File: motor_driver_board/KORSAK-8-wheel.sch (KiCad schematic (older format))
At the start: 24 parts, among them J1 Screw_Terminal_01x04, J2 Conn_01x02_Male, J3 Screw_Terminal_01x06, J4 Screw_Terminal_01x04, M1 Motor_DC, M2 Motor_DC, M3 Motor_DC, M4 Motor_DC, M5 Motor_DC, M6 Motor_DC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

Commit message: Откат прошлого коммита, т.к. это незаконченная версия
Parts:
- removed C1, C2, C3, C4, C5, C6, C7, C8: 10pF, symbol Device:C
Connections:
- net at M8.1 (+): now also U2.3 (1Y); no longer U2.6 (2Y)
- net at M8.2 (-): now also U2.6 (2Y); no longer U2.3 (1Y)
- net at U3.3 (1Y): now also M6.1 (+); no longer M6.2 (-)
- net at U3.6 (2Y): now also M6.2 (-); no longer M6.1 (+)
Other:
- moved on the sheet: J1, J4, M1, M2, M3, M4, M5, M6, M7, M8

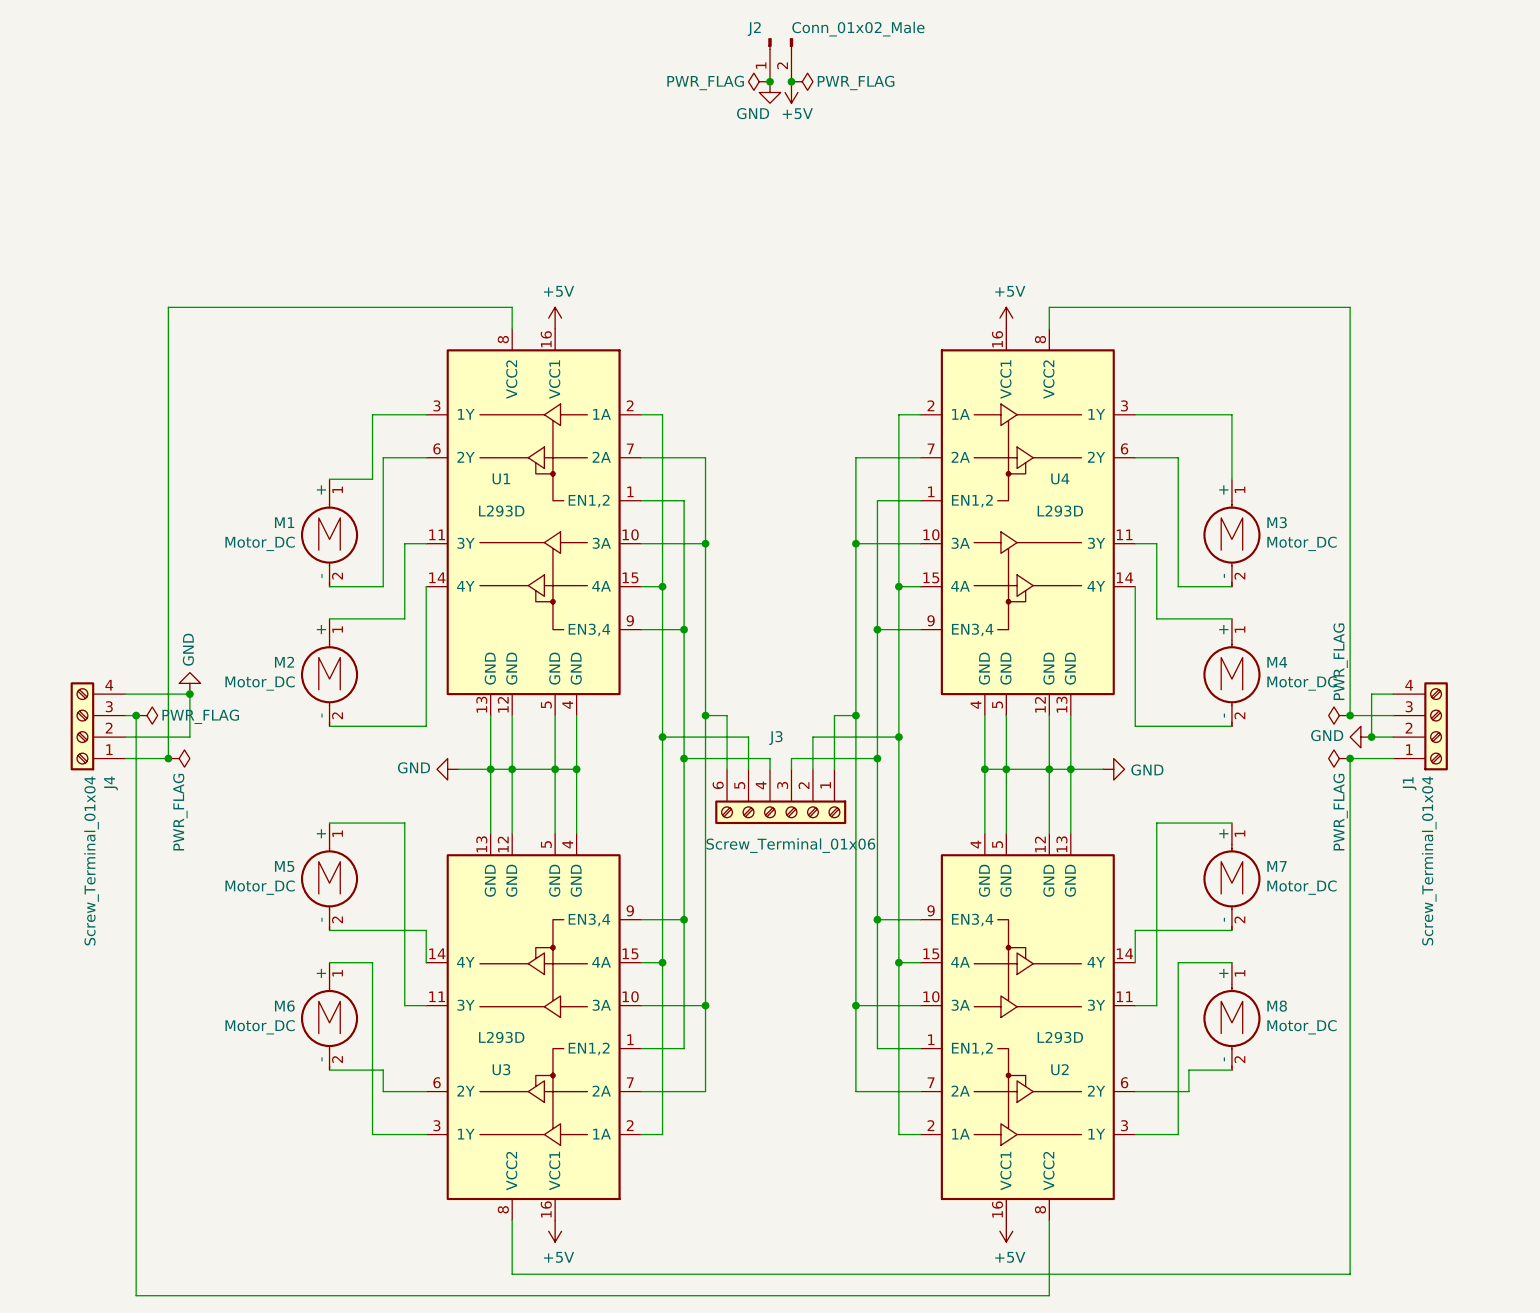
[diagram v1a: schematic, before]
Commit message: Добавил конденсаторы параллельно двигателям
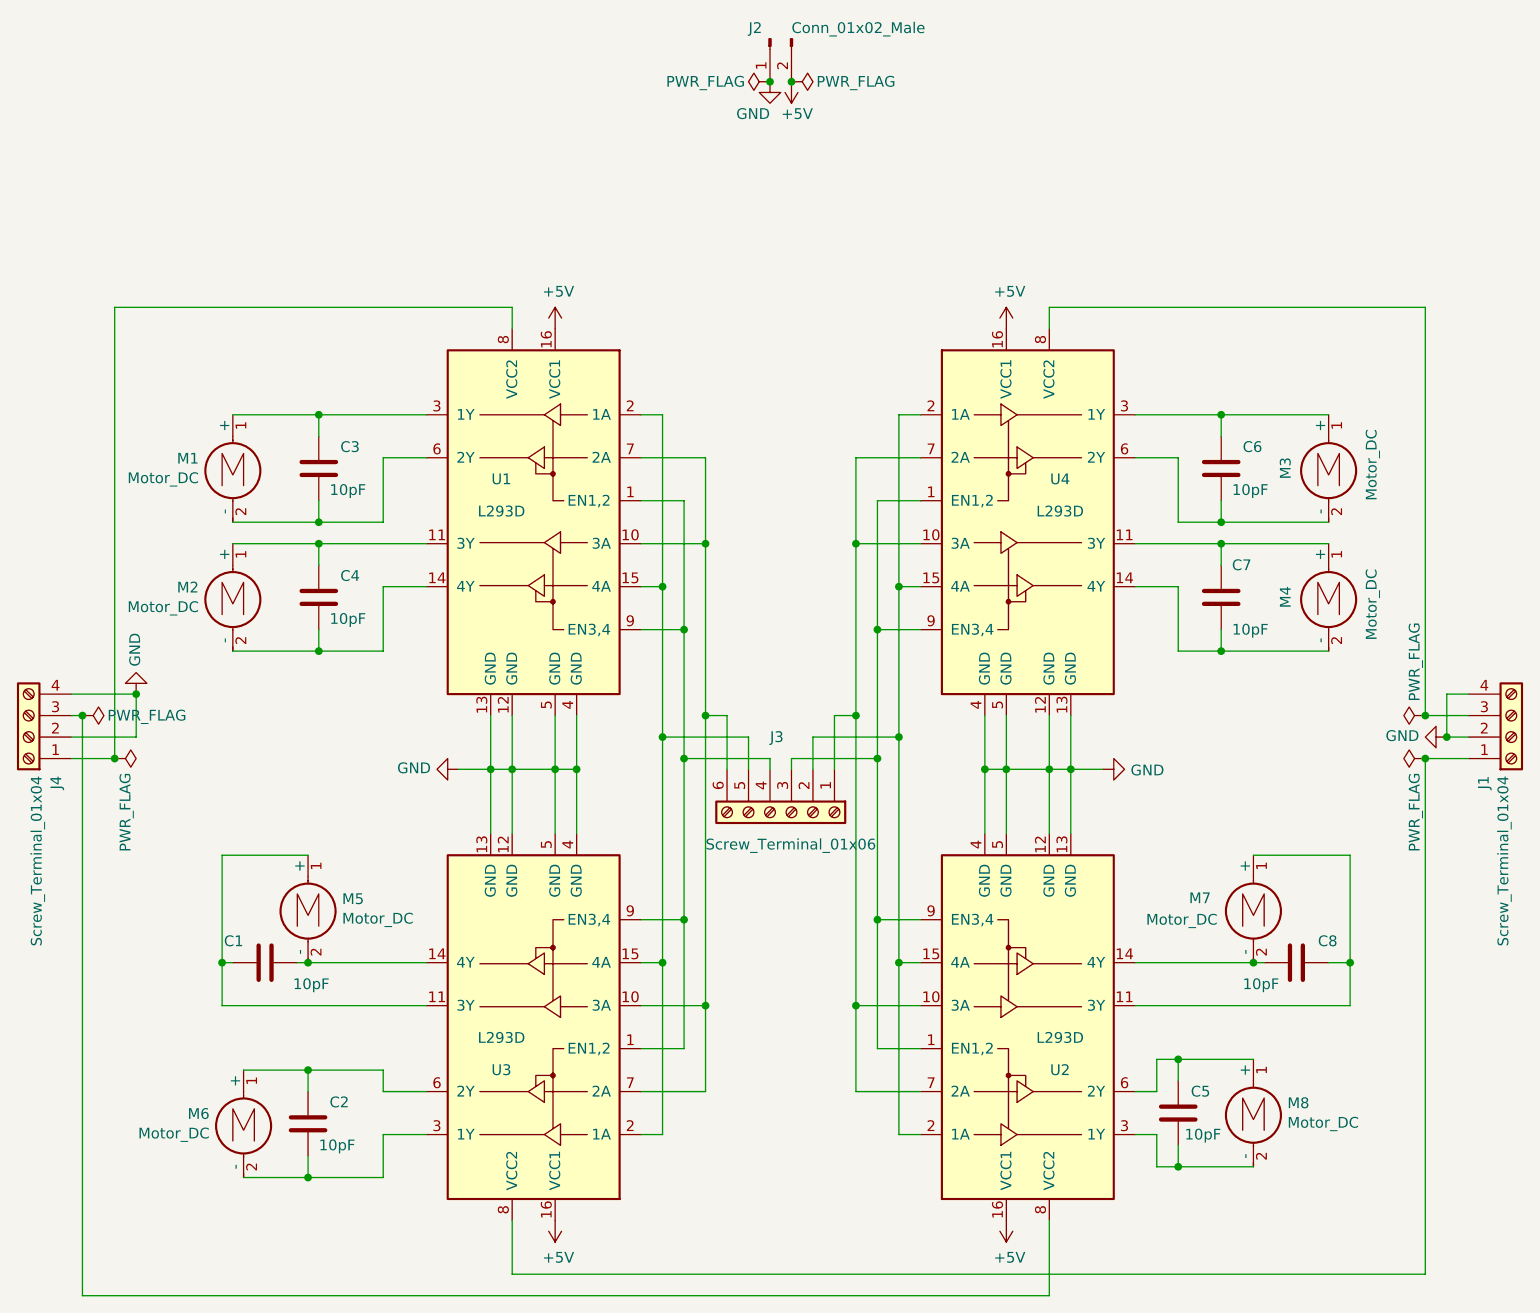
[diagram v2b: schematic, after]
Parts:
- added C1, C2, C3, C4, C5, C6, C7, C8: 10pF, symbol Device:C
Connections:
- net at M4.1 (+), U4.11 (3Y): now also C7.1
- net at M4.2 (-), U4.14 (4Y): now also C7.2
- net at M3.1 (+), U4.3 (1Y): now also C6.1
- net at M3.2 (-), U4.6 (2Y): now also C6.2
- net at M2.1 (+), U1.11 (3Y): now also C4.1
- net at M2.2 (-), U1.14 (4Y): now also C4.2
- net at M1.1 (+), U1.3 (1Y): now also C3.1
- net at M1.2 (-), U1.6 (2Y): now also C3.2
- net at M8.1 (+): now also U2.6 (2Y), C5.2; no longer U2.3 (1Y)
- net at M8.2 (-): now also U2.3 (1Y), C5.1; no longer U2.6 (2Y)
- net at M7.1 (+), U2.11 (3Y): now also C8.1
- net at M7.2 (-), U2.14 (4Y): now also C8.2
- net at M5.1 (+), U3.11 (3Y): now also C1.1
- net at M5.2 (-), U3.14 (4Y): now also C1.2
- net at U3.3 (1Y): now also M6.2 (-), C2.2; no longer M6.1 (+)
- net at U3.6 (2Y): now also M6.1 (+), C2.1; no longer M6.2 (-)
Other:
- moved on the sheet: J1, J4, M1, M2, M3, M4, M5, M6, M7, M8
